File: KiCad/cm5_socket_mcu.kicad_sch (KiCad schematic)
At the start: 9 parts, among them IC1 PI3USB102ZLEX, IC2 AZ1117CH2-3.3TRG1, IC3 AZ1117CH-1.8TRG1

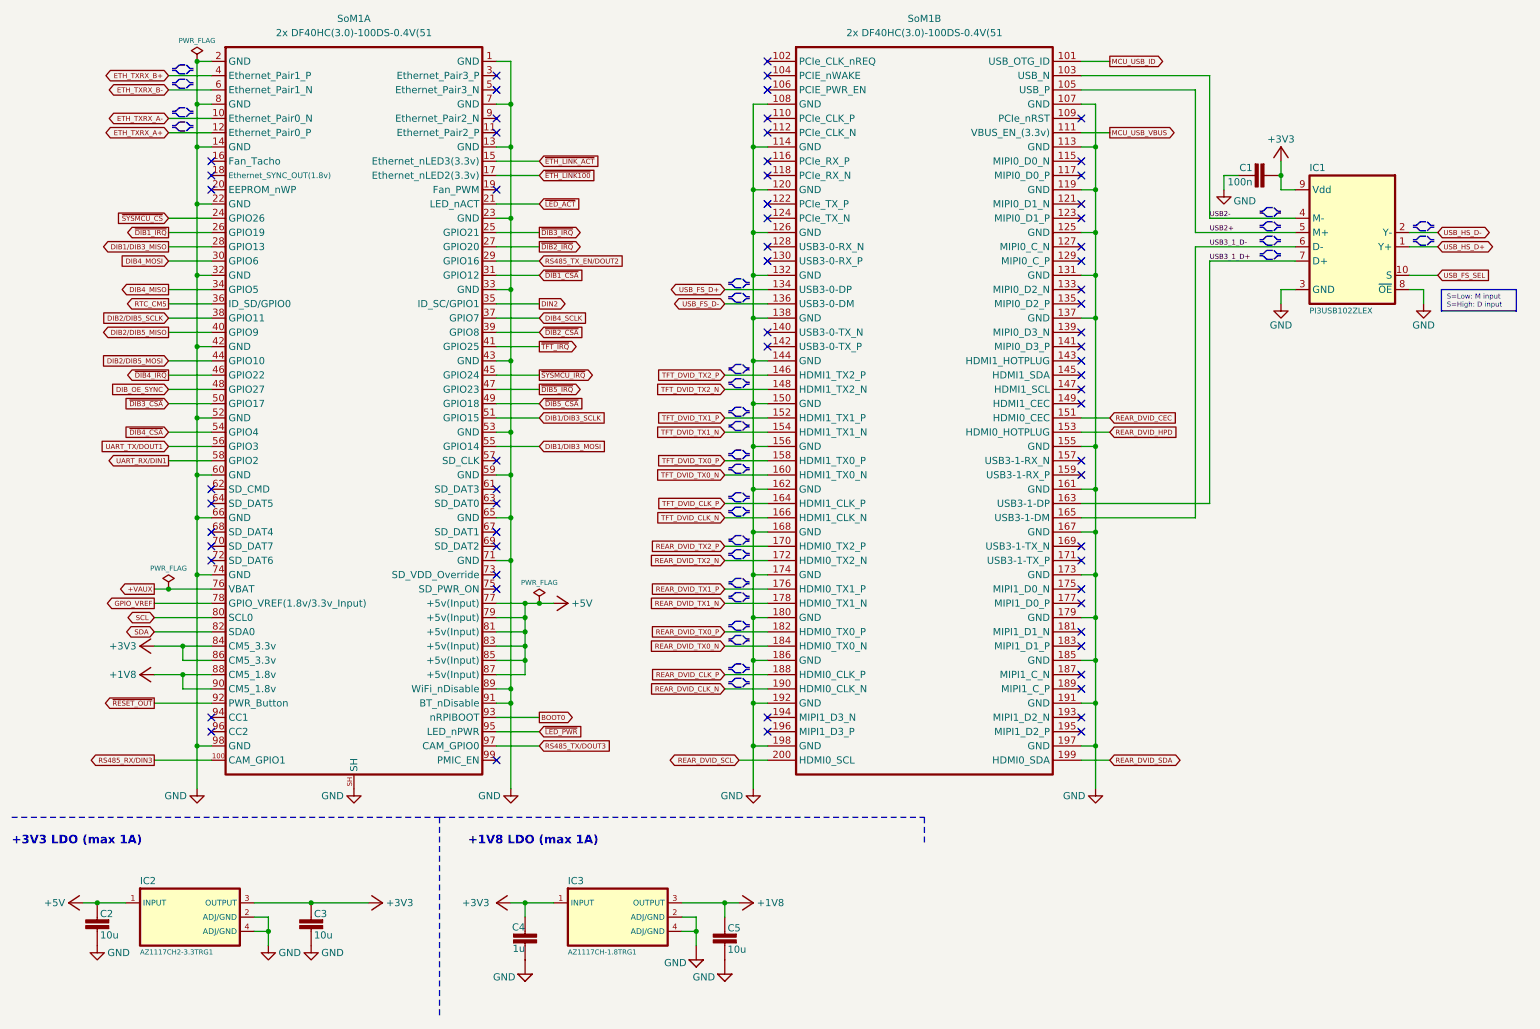
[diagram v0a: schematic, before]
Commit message: Split SoM footprint into two separate 100-pin connectors
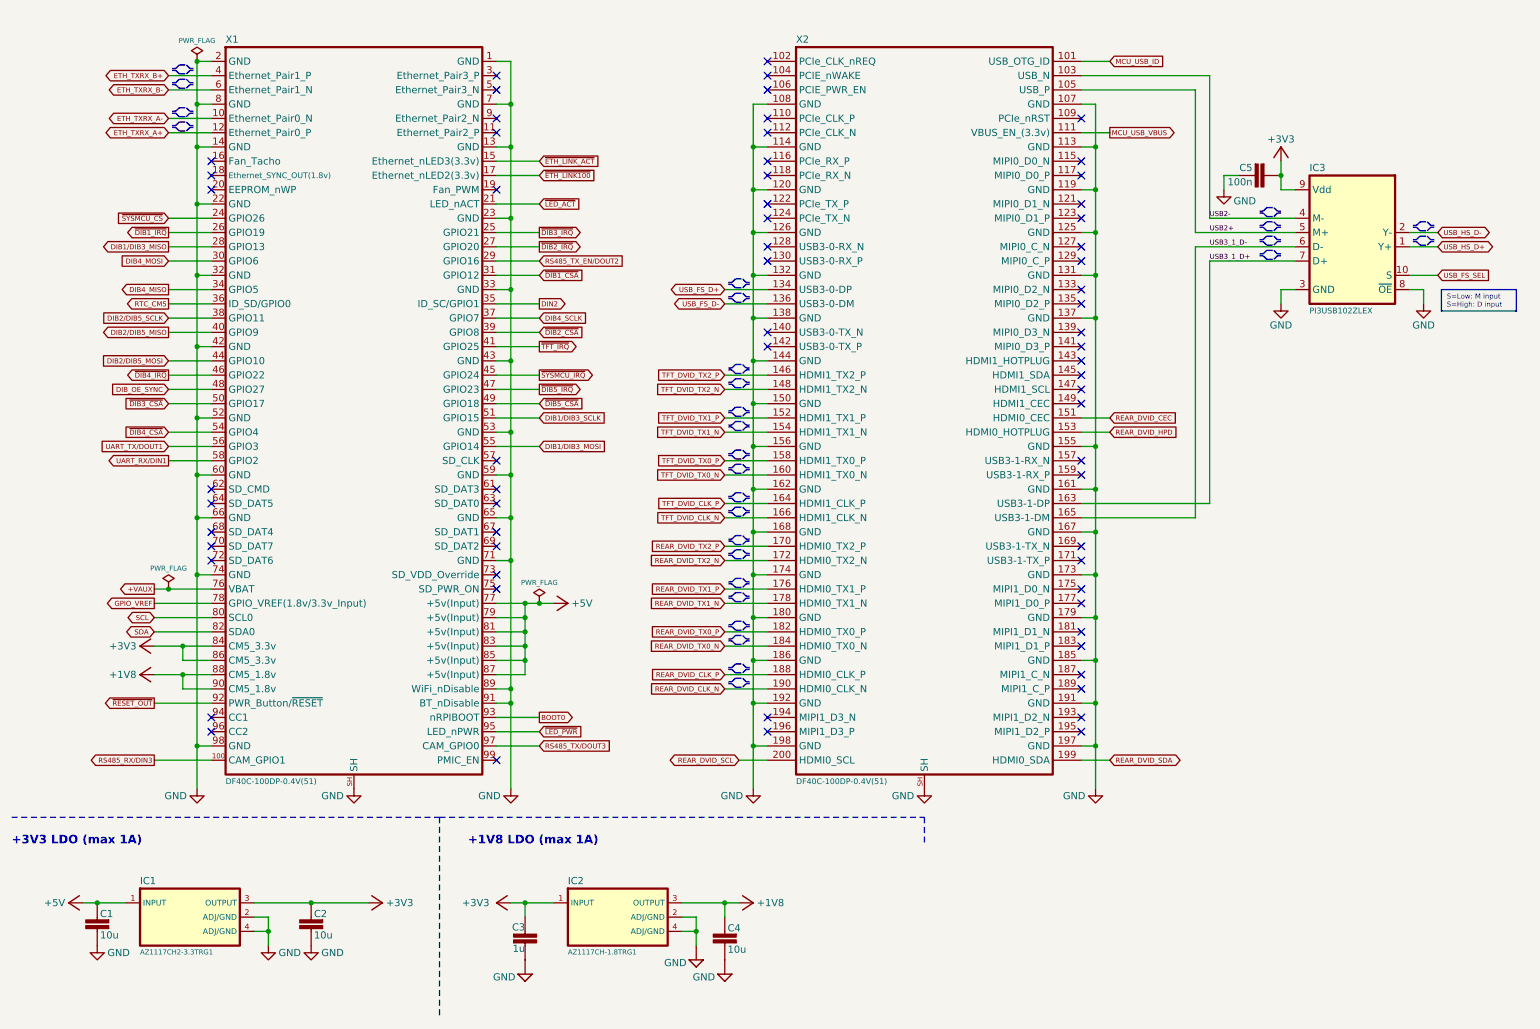
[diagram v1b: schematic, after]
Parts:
- removed SoM1: 2x DF40HC(3.0)-100DS-0.4V(51, PCM_EEZ_connectors:Raspberry-Pi-CM5 (SoM), symbol PCM_EEZ_connectors:Raspberry Pi CM5 (SoM)
- added X1: DF40C-100DP-0.4V(51), PCM_EEZ_connectors:Raspberry-Pi-CM5 (SoM)_Left, symbol PCM_EEZ_connectors:Raspberry Pi CM5 (SoM)_Left
- added X2: DF40C-100DP-0.4V(51), PCM_EEZ_connectors:Raspberry-Pi-CM5 (SoM)_Right, symbol PCM_EEZ_connectors:Raspberry Pi CM5 (SoM)_Right
- renumbered C2 to C1, C3 to C2, C4 to C3, C5 to C4, C1 to C5, IC2 to IC1, IC3 to IC2, IC1 to IC3
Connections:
- net +1V8: now also X1.88 (CM5_1.8v), X1.90 (CM5_1.8v)
- net +3V3: now also X1.84 (CM5_3.3v), X1.86 (CM5_3.3v)
- net +5V: now also X1.77 (+5v(Input)), X1.79 (+5v(Input)), X1.81 (+5v(Input)), X1.83 (+5v(Input)), X1.85 (+5v(Input)), X1.87 (+5v(Input))
- net +VAUX: now also X1.76 (VBAT)
- net BOOT0: now also X1.93 (nRPIBOOT)
- net DIB1/DIB3_MISO: now also X1.28 (GPIO13)
- net DIB1/DIB3_MOSI: now also X1.55 (GPIO14)
- net DIB1/DIB3_SCLK: now also X1.51 (GPIO15)
- net DIB2/DIB5_MISO: now also X1.40 (GPIO9)
- net DIB2/DIB5_MOSI: now also X1.44 (GPIO10)
- net DIB2/DIB5_SCLK: now also X1.38 (GPIO11)
- net DIB4_MISO: now also X1.34 (GPIO5)
- net DIB4_MOSI: now also X1.30 (GPIO6)
- net DIB4_SCLK: now also X1.37 (GPIO7)
- net DIB_OE_SYNC: now also X1.48 (GPIO27)
- net DIN2: now also X1.35 (ID_SC/GPIO1)
- net ETH_TXRX_A+: now also X1.12 (Ethernet_Pair0_P)
- net ETH_TXRX_A-: now also X1.10 (Ethernet_Pair0_N)
- net ETH_TXRX_B+: now also X1.4 (Ethernet_Pair1_P)
- net ETH_TXRX_B-: now also X1.6 (Ethernet_Pair1_N)
- net GND: now also X1.1 (GND), X1.13 (GND), X1.14 (GND), X1.2 (GND), X1.22 (GND), X1.23 (GND), X1.32 (GND), X1.33 (GND), X1.42 (GND), X1.43 (GND), X1.52 (GND), X1.53 (GND), X1.59 (GND), X1.60 (GND), X1.65 (GND), X1.66 (GND), X1.7 (GND), X1.71 (GND), X1.74 (GND), X1.8 (GND), X1.89 (WiFi_nDisable), X1.91 (BT_nDisable), X1.98 (GND), X1.SH, X2.107 (GND), X2.108 (GND), X2.113 (GND), X2.114 (GND), X2.119 (GND), X2.120 (GND), X2.125 (GND), X2.126 (GND), X2.131 (GND), X2.132 (GND), X2.137 (GND), X2.138 (GND), X2.144 (GND), X2.150 (GND), X2.155 (GND), X2.156 (GND), X2.161 (GND), X2.162 (GND), X2.167 (GND), X2.168 (GND), X2.173 (GND), X2.174 (GND), X2.179 (GND), X2.180 (GND), X2.185 (GND), X2.186 (GND), X2.191 (GND), X2.192 (GND), X2.197 (GND), X2.198 (GND), X2.SH
- net GPIO_VREF: now also X1.78 (GPIO_VREF(1.8v/3.3v_Input))
- net MCU_USB_ID: now also X2.101 (USB_OTG_ID)
- net MCU_USB_VBUS: now also X2.111 (VBUS_EN_(3.3v))
- net REAR_DVID_CEC: now also X2.151 (HDMI0_CEC)
- net REAR_DVID_CLK_N: now also X2.190 (HDMI0_CLK_N)
- net REAR_DVID_CLK_P: now also X2.188 (HDMI0_CLK_P)
- net REAR_DVID_HPD: now also X2.153 (HDMI0_HOTPLUG)
- net REAR_DVID_SCL: now also X2.200 (HDMI0_SCL)
- net REAR_DVID_SDA: now also X2.199 (HDMI0_SDA)
- net REAR_DVID_TX0_N: now also X2.184 (HDMI0_TX0_N)
- net REAR_DVID_TX0_P: now also X2.182 (HDMI0_TX0_P)
- net REAR_DVID_TX1_N: now also X2.178 (HDMI0_TX1_N)
- net REAR_DVID_TX1_P: now also X2.176 (HDMI0_TX1_P)
- net REAR_DVID_TX2_N: now also X2.172 (HDMI0_TX2_N)
- net REAR_DVID_TX2_P: now also X2.170 (HDMI0_TX2_P)
- net RS485_RX/DIN3: now also X1.100 (CAM_GPIO1)
- net RS485_TX_EN/DOUT2: now also X1.29 (GPIO16)
- net RS485_TX/DOUT3: now also X1.97 (CAM_GPIO0)
- net RTC_CM5: now also X1.36 (ID_SD/GPIO0)
- net SCL: now also X1.80 (SCL0)
- net SDA: now also X1.82 (SDA0)
- net TFT_DVID_CLK_N: now also X2.166 (HDMI1_CLK_N)
- net TFT_DVID_CLK_P: now also X2.164 (HDMI1_CLK_P)
- net TFT_DVID_TX0_N: now also X2.160 (HDMI1_TX0_N)
- net TFT_DVID_TX0_P: now also X2.158 (HDMI1_TX0_P)
- net TFT_DVID_TX1_N: now also X2.154 (HDMI1_TX1_N)
- net TFT_DVID_TX1_P: now also X2.152 (HDMI1_TX1_P)
- net TFT_DVID_TX2_N: now also X2.148 (HDMI1_TX2_N)
- net TFT_DVID_TX2_P: now also X2.146 (HDMI1_TX2_P)
- net UART_RX/DIN1: now also X1.58 (GPIO2)
- net UART_TX/DOUT1: now also X1.56 (GPIO3)
- net USB2+: now also X2.105 (USB_P)
- net USB2-: now also X2.103 (USB_N)
- net USB3_1_D+: now also X2.163 (USB3-1-DP)
- net USB3_1_D-: now also X2.165 (USB3-1-DM)
- net USB_FS_D+: now also X2.134 (USB3-0-DP)
- net USB_FS_D-: now also X2.136 (USB3-0-DM)
- net ~{DIB1_CSA}: now also X1.31 (GPIO12)
- net ~{DIB1_IRQ}: now also X1.26 (GPIO19)
- net ~{DIB2_CSA}: now also X1.39 (GPIO8)
- net ~{DIB2_IRQ}: now also X1.27 (GPIO20)
- net ~{DIB3_CSA}: now also X1.50 (GPIO17)
- net ~{DIB3_IRQ}: now also X1.25 (GPIO21)
- net ~{DIB4_CSA}: now also X1.54 (GPIO4)
- net ~{DIB4_IRQ}: now also X1.46 (GPIO22)
- net ~{DIB5_CSA}: now also X1.49 (GPIO18)
- net ~{DIB5_IRQ}: now also X1.47 (GPIO23)
- net ~{ETH_LINK100}: now also X1.17 (Ethernet_nLED2(3.3v))
- net ~{ETH_LINK_ACT}: now also X1.15 (Ethernet_nLED3(3.3v))
- net ~{LED_ACT}: now also X1.21 (LED_nACT)
- net ~{LED_PWR}: now also X1.95 (LED_nPWR)
- net ~{RESET_OUT}: now also X1.92 (PWR_Button/~{RESET})
- net ~{SYSMCU_CS}: now also X1.24 (GPIO26)
- net ~{SYSMCU_IRQ}: now also X1.45 (GPIO24)
- net ~{TFT_IRQ}: now also X1.41 (GPIO25)

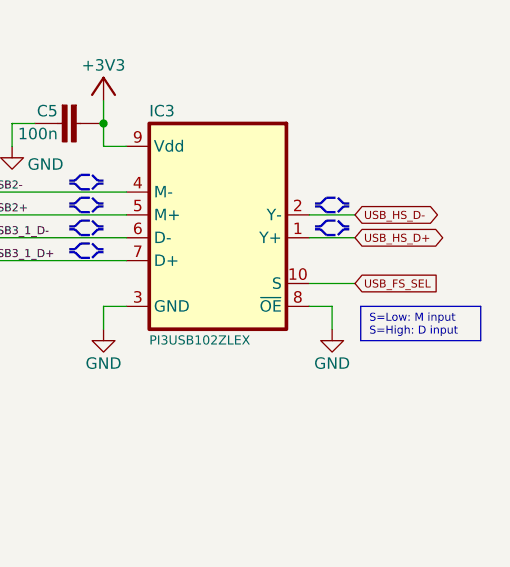
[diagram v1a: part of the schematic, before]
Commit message: Rename USB_FS_SEL to USB_HS_SEL
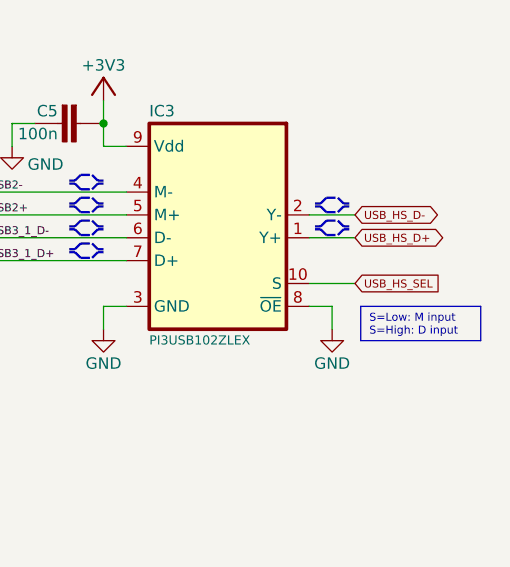
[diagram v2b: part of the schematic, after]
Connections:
- net USB_FS_SEL renamed USB_HS_SEL
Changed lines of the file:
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@@
 		)
 	)
-	(global_label "USB_FS_SEL"
+	(global_label "USB_HS_SEL"
 		(shape input)
 		(at 269.24 63.5 0)
@@
 		)
 		(property "Intersheetrefs" "${INTERSHEET_REFS}"
-			(at 278.8726 63.5 0)
+			(at 279.0419 63.5 0)
 			(hide yes)
 			(show_name no)

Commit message: #20
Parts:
- added JP1: (no value), PCM_EEZ_SMD:JP3 shorted (0603), symbol PCM_EEZ_unsorted:JP3 shorted
- added R1: 10K, PCM_EEZ_passives:R_0402_1005Metric, symbol PCM_EEZ_passives:R-EU
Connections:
- net +3V3: now also JP1.NO
- net GND: now also JP1.NC
- net USB_HS_SEL: now also R1.2
- new net: JP1.COM, R1.1
